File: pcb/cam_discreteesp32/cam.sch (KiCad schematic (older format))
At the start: 106 parts, among them J1 Conn_Coaxial, J2 Power In, J3 CONN_PRG_ESP, J4 Conn_01x24_Male, J5 SIM_Card, J6 Conn_Coaxial, Q1 IRLML6402, SW1 SW_Push, SW2 SW_Push, U1 TPS22810, U10 W25Q128JVS, U11 LY68L6400, U12 SRV05-4, U13 SIM800C, U2 FDC610, U3 XC6206-12, U4 XC6206-28, U5 LTC3103, U6 INA226, U7 ESP32-D0WD, U8 MP2307, U9 MAX7321, Y1 32.768kHz, Y2 40Mhz

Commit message: Finished PCB for ESP32-S2
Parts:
- removed J3: CONN_PRG_ESP, Connector_JST:JST_XH_B5B-XH-A_1x05_P2.50mm_Vertical, symbol Connector:Conn_01x05_Male
- removed SW1, SW2: SW_Push, Elktown Footprints:smd_2pole_pushbtn, symbol Switch:SW_Push
- removed U7: ESP32-D0WD, Elktown Footprints:QFN35P500X500X90-49N, symbol elktown-labs:ESP32-D0WD
- removed U9: MAX7321, Package_SO:QSOP-16_3.9x4.9mm_P0.635mm, symbol elktown-labs:MAX7321
- added J3: PRGR, Connector_PinHeader_1.27mm:PinHeader_2x03_P1.27mm_Vertical, symbol Connector_Generic:Conn_02x03_Odd_Even
- added J7: JTAG, Connector_PinHeader_1.27mm:PinHeader_2x05_P1.27mm_Vertical, symbol Connector_Generic:Conn_02x05_Odd_Even
- added R28: 0, Resistor_SMD:R_0603_1608Metric, symbol Device:R_Small_US
- added R29, R32: 10k, Resistor_SMD:R_0603_1608Metric, symbol Device:R_Small_US
- added R30, R31: 4.7k, Resistor_SMD:R_0603_1608Metric, symbol Device:R_Small_US
- added U7: ESP32-S2, Package_DFN_QFN:QFN-56-1EP_7x7mm_P0.4mm_EP5.6x5.6mm_ThermalVias, symbol elktown-labs:ESP32-S2
- C14, C15: value 270p -> 1u
- C20: footprint Capacitor_SMD:C_1206_3216Metric -> Capacitor_SMD:C_0603_1608Metric
- C23, C6: footprint Capacitor_SMD:C_0805_2012Metric -> Capacitor_SMD:C_0603_1608Metric
- C28: value 1u -> 100n; footprint Capacitor_SMD:C_0805_2012Metric -> Capacitor_SMD:C_0603_1608Metric
- C3: value 3.3n -> 100p
- C34: value 100p -> 100n
- C4: value 10n -> 1u
- R1: value 20k -> 0
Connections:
- net SD_CLK is gone; now on net SPICLK: U10.6 (CLK)
- net 3V3: now also C15.1, C28.1, C3.1, C4.1, J3.2 (Pin_2), J7.1 (Pin_1), R30.1, R31.1, U7.1 (VDDA_1), U7.20 (VDD3P3_RTC), U7.27 (VDD3P3_RTC_IO), U7.3 (VDD3P3_1), U7.4 (VDD3P3_2), U7.45 (VDD3P3_CPU), U7.51 (VDDA_2), U7.54 (VDDA_3); no longer C34.1, C39.1
- net CAM_EN: now also U7.26 (GPIO20)
- net CAM_RST: now also U7.28 (GPIO21)
- net CSI_D0: now also U7.16 (GPIO11)
- net CSI_D1: now also U7.18 (GPIO13)
- net CSI_D2: now also U7.19 (GPIO14)
- net CSI_D3: now also U7.17 (GPIO12)
- net CSI_D4: now also U7.15 (GPIO10)
- net CSI_D5: now also U7.13 (GPIO8)
- net CSI_D6: now also U7.12 (GPIO7)
- net CSI_D7: now also U7.10 (GPIO5)
- net CSI_HSYNC: now also U7.9 (GPIO4)
- net CSI_MCLK: now also U7.11 (GPIO6)
- net CSI_PCLK: now also U7.14 (GPIO9)
- net CSI_VSYNC: now also U7.8 (GPIO3)
- net GND: now also C14.2, C15.2, C3.2, J3.4 (Pin_4), J7.3 (Pin_3), J7.5 (Pin_5), J7.7 (Pin_7), J7.9 (Pin_9), R32.2, U7.57 (GND)
- net GSM_PWRKEY: now also U7.37 (GPIO33)
- net GSM_RX: now also U7.24 (DAC_2)
- net GSM_TX: now also U7.23 (DAC_1)
- net PRGRM: now also J3.6 (Pin_6), U7.5 (GPIO0)
- net PRGR_RX: now also R1.1, J3.5 (Pin_5)
- net PRGR_TX: now also J3.3 (Pin_3), R28.1
- net RADIO_EN: now also U7.25 (GPIO19)
- net SD_DATA0: now also U7.36 (SPID)
- net SD_DATA1: now also U7.35 (SPIQ)
- net SD_DATA2: now also U7.32 (SPIWP)
- net SD_DATA3: now also U7.31 (SPIHD)
- net VDD_SDIO: now also C14.1, C34.1, R29.2, U7.30 (VDD_SPI); no longer C28.1
- net ~RST: now also C39.1, J3.1 (Pin_1), U7.56 (CHIP_PU)
- net at U13.6 (UART1_DTR): now also R32.1
- net LED2: now reaches R18.1
- net LED2: now also U7.38 (GPIO34)
- net XTAL32P: now reaches C7.2, R3.1, Y1.1
- net XTAL32P: now also U7.21 (XTAL_32K_P)
- net XTAL32N: now reaches C12.2, R3.2, Y1.2
- net XTAL32N: now also U7.22 (XTAL_32K_N)
- net at C2.1, L1.1: now also U7.2 (LNA_IN)
- net XTALN: now reaches C10.2, Y2.1
- net XTALN: now also U7.52 (XTAL_N)
- net XTALP: now reaches R5.2
- net XTALP: now also U7.53 (XTAL_P)
- net at R1.2: now also U7.49 (U0RXD); no longer C3.2
- net LED1: now reaches R19.1
- net LED1: now also U7.39 (GPIO35)
- net PSRAM_CE renamed SPICS1
- net SPICS1: now also U7.29 (SPICS1)
- net PSRAM_SCLK renamed SPICLK
- net SPICLK: now also U7.34 (SPICLK)
- removed net SCL: J4.20 (Pin_20), R14.2, U6.5 (SCL)
- removed net SDA: J4.22 (Pin_22), R11.2, U6.4 (SDA)
- net SD_CMD renamed SPICS0
- net SPICS0: now also R29.1, U7.33 (SPICS0)
- new net: R28.2, U7.48 (U0TXD)
- new net SCL_AUX: R31.2, U6.5 (SCL), U7.40 (GPIO36)
- new net SCL_CAM: J4.20 (Pin_20), R11.2, U7.7 (GPIO2)
- new net SDA_AUX: R30.2, U6.4 (SDA), U7.41 (GPIO37)
- new net SDA_CAM: J4.22 (Pin_22), R14.2, U7.6 (GPIO1)
- new net TCK: J7.4 (Pin_4), U7.43 (MTCK)
- new net TDI: J7.8 (Pin_8), U7.46 (MTDI)
- new net TDO: J7.6 (Pin_6), U7.44 (MTD0)
- new net TMS: J7.2 (Pin_2), U7.47 (MTMS)
- no-connect marks 31 -> 30
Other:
- moved on the sheet: C1, C10, C11, C12, C13, C14, C18, C19, C2, C20, C21, C23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

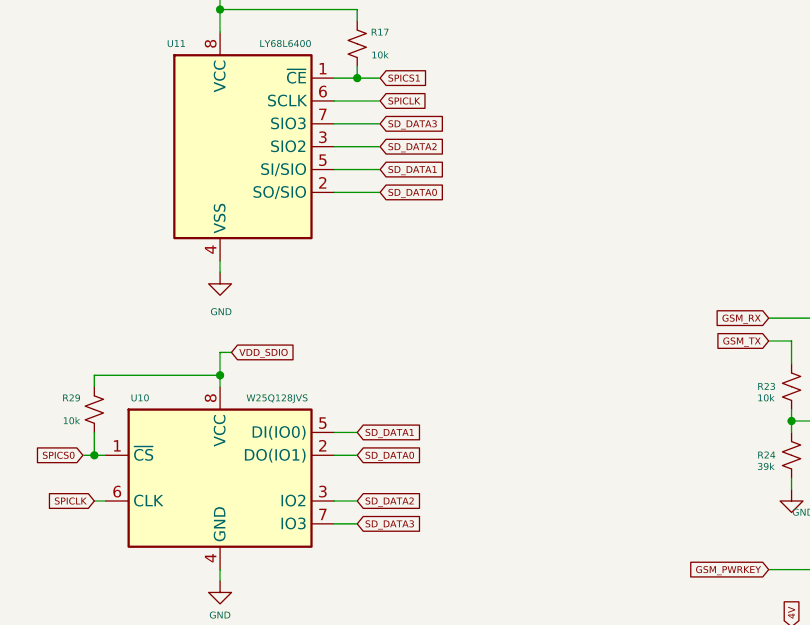
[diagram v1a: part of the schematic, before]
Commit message: Fixed connection / layout of flash / ram chips
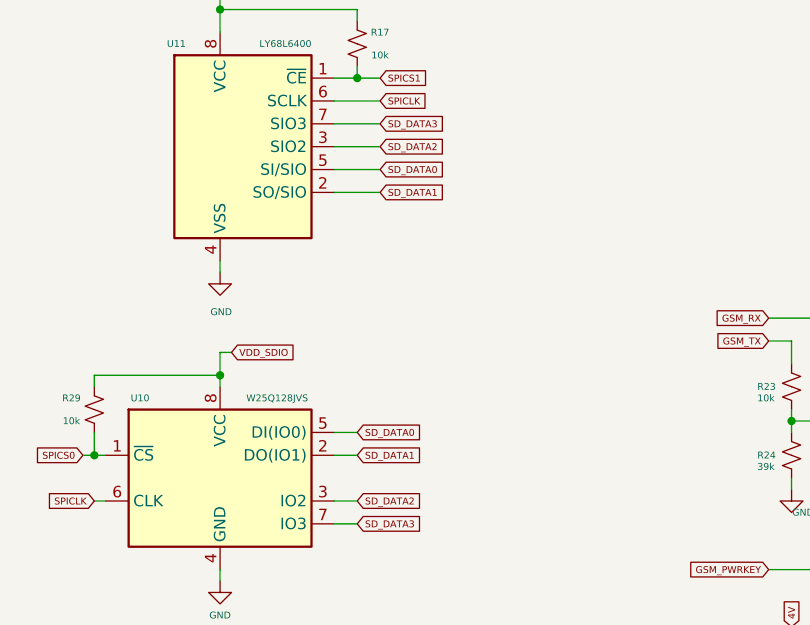
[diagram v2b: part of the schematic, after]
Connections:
- net SD_DATA0: now also U10.5 (DI(IO0)), U11.5 (SI/SIO); no longer U10.2 (DO(IO1)), U11.2 (SO/SIO)
- net SD_DATA1: now also U10.2 (DO(IO1)), U11.2 (SO/SIO); no longer U10.5 (DI(IO0)), U11.5 (SI/SIO)
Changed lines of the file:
@@
 Wire Wire Line
 	10600 4500 10700 4500
-Text GLabel 10700 4500 2    30   Input ~ 0
+Text GLabel 10800 3450 2    30   Input ~ 0
 SD_DATA1
 Text GLabel 10800 3350 2    30   Input ~ 0
-SD_DATA1
-Text GLabel 10800 3450 2    30   Input ~ 0
-SD_DATA0
-Text GLabel 10700 4600 2    30   Input ~ 0
 SD_DATA0
 Text GLabel 9550 4800 0    30   Input ~ 0
@@
 Wire Wire Line
 	10300 5800 10350 5800
+Text GLabel 10700 4500 2    30   Input ~ 0
+SD_DATA0
+Text GLabel 10700 4600 2    30   Input ~ 0
+SD_DATA1
 $EndSCHEMATC
